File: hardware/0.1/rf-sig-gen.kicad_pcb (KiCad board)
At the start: 4 copper layers, 50 x 22.9 mm, 89 parts, among them J1 Feather, J2 SMA, U1 MAX2871, U2 LP5912, U3 MIC5366-1.8, U4 SKY12347-362LF, U5 TRF37A75, U6 AD8319, U7 STP08CP05

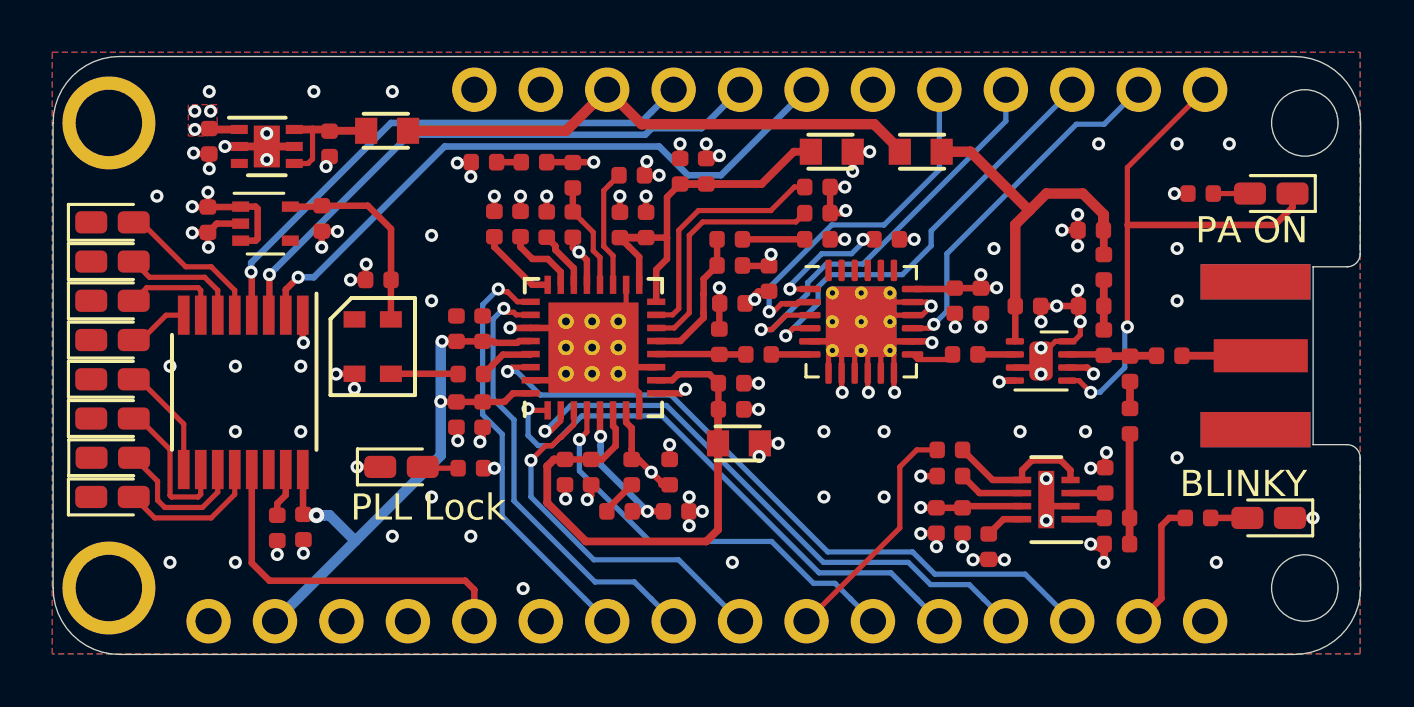
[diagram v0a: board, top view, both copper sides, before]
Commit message: update schematic
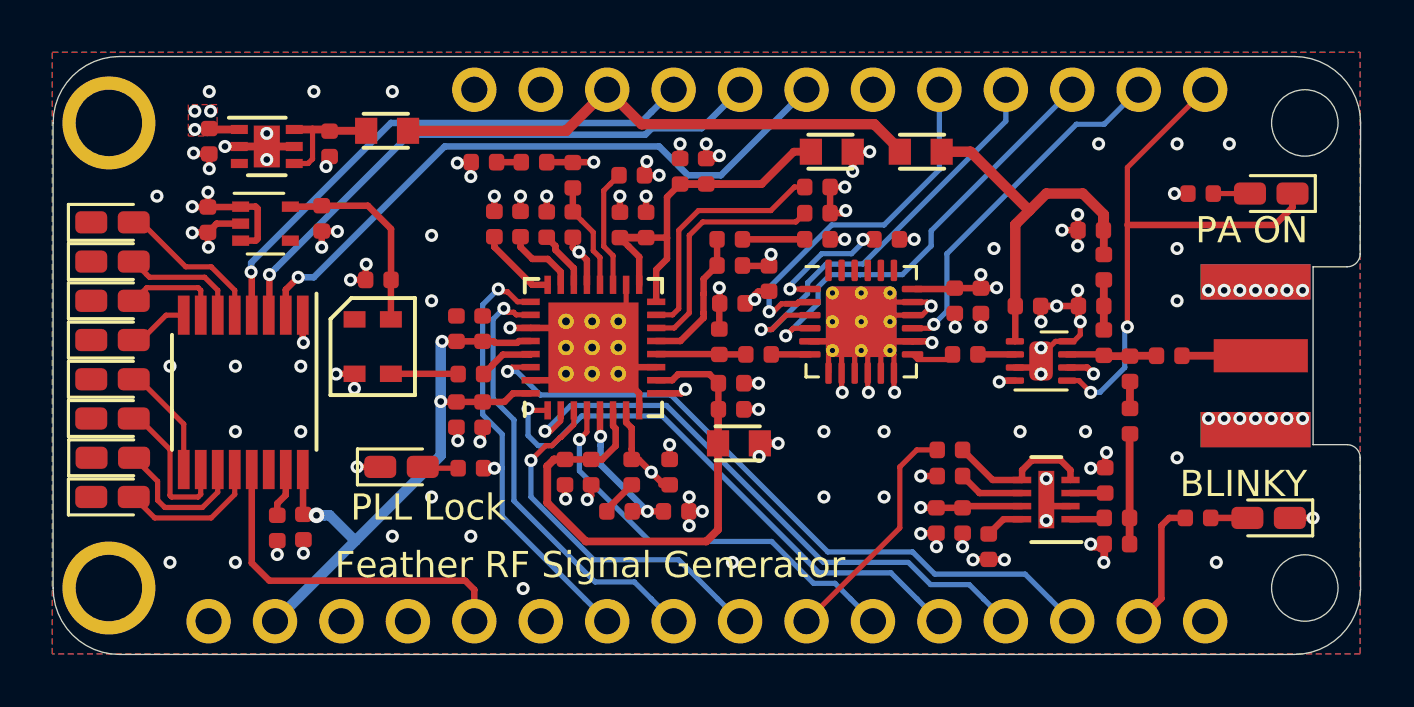
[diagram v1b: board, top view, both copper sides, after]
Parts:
- added G***: LOGO, josh-logos:OSHW_Logo_3.6x3.6_F.Mask, F.Cu at (137.5, 112.4)
- added REF**: Josh Details, josh-logos:josh-details, B.Cu at (148.1, 112.8)
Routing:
- net GND: vias 108 -> 122
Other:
- board text added: "DC to Daylight"
- board text added: "Feather RF Signal Generator"
